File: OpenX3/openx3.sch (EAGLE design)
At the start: 34 parts, among them IC1 24AA256SN, J1 BM20B-SRDS-G-TF(LF)(SN), J2 SM12B-SRSS-TB(LF)(SN), J3 53398-0271, J4 1734260-3, U1 LC4256V-75TN100CTQFP100-L, U2 AM29F016D-70EF, U3 AM29F002BB90EI

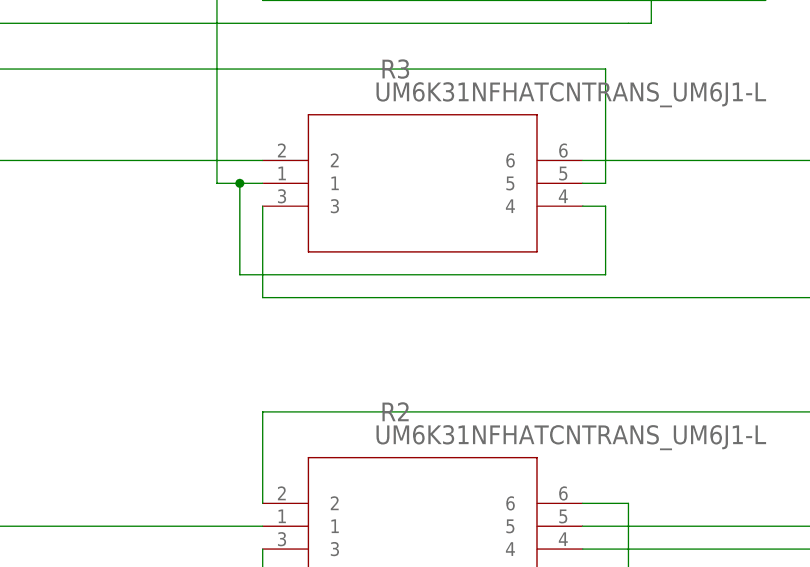
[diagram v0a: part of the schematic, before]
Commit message: Make correction where resistor arrays were not connected to +3v3, previous net name was N$4 before connecting to +3v3
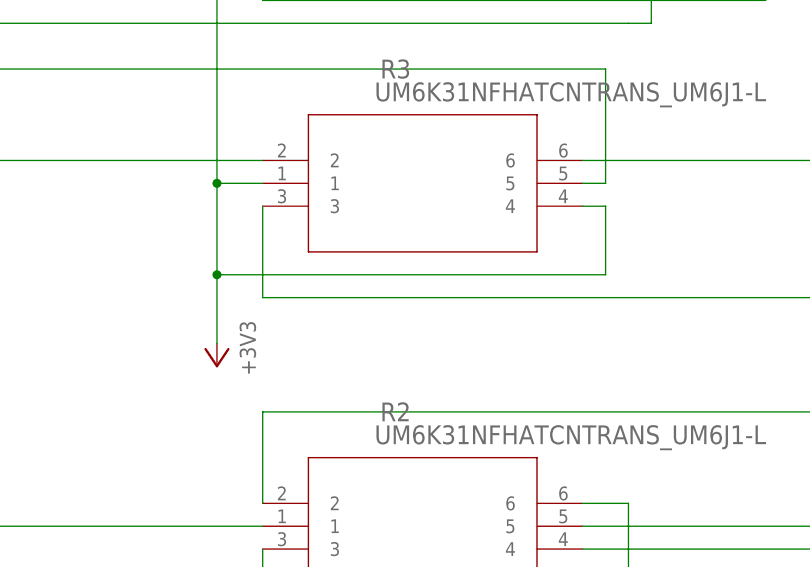
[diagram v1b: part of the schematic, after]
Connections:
- removed net N$4: R3.1, R3.4, R4.1, R4.4, R7.2, RN2A.1, RN2B.1, RN2C.1, RN2D.1
- net +3V3: now also R3.1, R3.4, R4.1, R4.4, R7.2, RN2A.1, RN2B.1, RN2C.1, RN2D.1
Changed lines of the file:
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@@
 <?xml version="1.0" encoding="utf-8"?>
 <!DOCTYPE eagle SYSTEM "eagle.dtd">
-<eagle version="9.3.1">
+<eagle version="9.5.0">
 <drawing>
 <settings>
@@
 <part name="SUPPLY12" library="supply2" library_urn="urn:adsk.eagle:library:372" deviceset="GND" device=""/>
 <part name="J1" library="BM20B-SRDS-G-TFLFSN" deviceset="BM20B-SRDS-G-TF(LF)(SN)" device=""/>
+<part name="+3V2" library="supply1" library_urn="urn:adsk.eagle:library:371" deviceset="+3V3" device=""/>
 </parts>
 <sheets>
@@
 <attribute name="NAME" x="-52.07" y="48.26" size="1.778" layer="95" align="center-left"/>
 <attribute name="VALUE" x="-52.07" y="45.72" size="1.778" layer="96" align="center-left"/>
+</instance>
+<instance part="+3V2" gate="G$1" x="-86.36" y="124.46" smashed="yes" rot="R180">
+<attribute name="VALUE" x="-83.82" y="129.54" size="1.778" layer="96" rot="R270"/>
 </instance>
 </instances>
@@
 <junction x="-99.06" y="213.36"/>
 <label x="-83.82" y="246.38" size="1.778" layer="95" rot="R90"/>
-</segment>
-</net>
-<net name="N$4" class="0">
-<segment>
-<pinref part="R4" gate="A" pin="4"/>
-<wire x1="-43.18" y1="175.26" x2="-45.72" y2="175.26" width="0.1524" layer="91"/>
-<wire x1="-43.18" y1="167.64" x2="-43.18" y2="175.26" width="0.1524" layer="91"/>
-<wire x1="-83.82" y1="167.64" x2="-43.18" y2="167.64" width="0.1524" layer="91"/>
-<pinref part="R4" gate="A" pin="1"/>
-<wire x1="-81.28" y1="177.8" x2="-83.82" y2="177.8" width="0.1524" layer="91"/>
-<wire x1="-83.82" y1="177.8" x2="-83.82" y2="167.64" width="0.1524" layer="91"/>
-<junction x="-83.82" y="177.8"/>
-<pinref part="R3" gate="A" pin="4"/>
-<wire x1="-43.18" y1="142.24" x2="-45.72" y2="142.24" width="0.1524" layer="91"/>
-<wire x1="-43.18" y1="134.62" x2="-43.18" y2="142.24" width="0.1524" layer="91"/>
-<wire x1="-83.82" y1="134.62" x2="-43.18" y2="134.62" width="0.1524" layer="91"/>
-<pinref part="R3" gate="A" pin="1"/>
-<wire x1="-81.28" y1="144.78" x2="-83.82" y2="144.78" width="0.1524" layer="91"/>
-<wire x1="-83.82" y1="144.78" x2="-83.82" y2="134.62" width="0.1524" layer="91"/>
-<junction x="-83.82" y="144.78"/>
-<wire x1="-83.82" y1="144.78" x2="-86.36" y2="144.78" width="0.1524" layer="91"/>
-<wire x1="-86.36" y1="144.78" x2="-86.36" y2="177.8" width="0.1524" layer="91"/>
-<wire x1="-86.36" y1="177.8" x2="-83.82" y2="177.8" width="0.1524" layer="91"/>
-<junction x="-86.36" y="177.8"/>
-<wire x1="-86.36" y1="198.12" x2="-86.36" y2="177.8" width="0.1524" layer="91"/>
-<pinref part="RN2" gate="D" pin="1"/>
-<wire x1="-121.92" y1="198.12" x2="-86.36" y2="198.12" width="0.1524" layer="91"/>
-<junction x="-121.92" y="198.12"/>
-<pinref part="RN2" gate="C" pin="1"/>
-<wire x1="-127" y1="198.12" x2="-121.92" y2="198.12" width="0.1524" layer="91"/>
-<junction x="-127" y="198.12"/>
-<pinref part="RN2" gate="B" pin="1"/>
-<wire x1="-132.08" y1="198.12" x2="-127" y2="198.12" width="0.1524" layer="91"/>
-<junction x="-132.08" y="198.12"/>
-<pinref part="RN2" gate="A" pin="1"/>
-<wire x1="-137.16" y1="198.12" x2="-132.08" y2="198.12" width="0.1524" layer="91"/>
-<junction x="-137.16" y="198.12"/>
-<pinref part="R7" gate="G$1" pin="2"/>
-<wire x1="-149.86" y1="198.12" x2="-137.16" y2="198.12" width="0.1524" layer="91"/>
 </segment>
 </net>
@@
 <label x="297.18" y="-132.08" size="1.778" layer="95"/>
 </segment>
-</net>
+<segment>
+<pinref part="R4" gate="A" pin="4"/>
+<wire x1="-43.18" y1="175.26" x2="-45.72" y2="175.26" width="0.1524" layer="91"/>
+<wire x1="-43.18" y1="167.64" x2="-43.18" y2="175.26" width="0.1524" layer="91"/>
+<wire x1="-83.82" y1="167.64" x2="-43.18" y2="167.64" width="0.1524" layer="91"/>
+<pinref part="R4" gate="A" pin="1"/>
+<wire x1="-81.28" y1="177.8" x2="-83.82" y2="177.8" width="0.1524" layer="91"/>
+<wire x1="-83.82" y1="177.8" x2="-83.82" y2="167.64" width="0.1524" layer="91"/>
+<junction x="-83.82" y="177.8"/>
+<pinref part="R3" gate="A" pin="4"/>
+<wire x1="-43.18" y1="142.24" x2="-45.72" y2="142.24" width="0.1524" layer="91"/>
+<wire x1="-43.18" y1="134.62" x2="-43.18" y2="142.24" width="0.1524" layer="91"/>
+<wire x1="-86.36" y1="134.62" x2="-43.18" y2="134.62" width="0.1524" layer="91"/>
+<pinref part="R3" gate="A" pin="1"/>
+<wire x1="-81.28" y1="144.78" x2="-86.36" y2="144.78" width="0.1524" layer="91"/>
+<wire x1="-86.36" y1="144.78" x2="-86.36" y2="134.62" width="0.1524" layer="91"/>
+<junction x="-86.36" y="144.78"/>
+<wire x1="-86.36" y1="144.78" x2="-86.36" y2="177.8" width="0.1524" layer="91"/>
+<wire x1="-86.36" y1="177.8" x2="-83.82" y2="177.8" width="0.1524" layer="91"/>
+<junction x="-86.36" y="177.8"/>
+<wire x1="-86.36" y1="198.12" x2="-86.36" y2="177.8" width="0.1524" layer="91"/>
+<pinref part="RN2" gate="D" pin="1"/>
+<wire x1="-121.92" y1="198.12" x2="-86.36" y2="198.12" width="0.1524" layer="91"/>
+<junction x="-121.92" y="198.12"/>
+<pinref part="RN2" gate="C" pin="1"/>
+<wire x1="-127" y1="198.12" x2="-121.92" y2="198.12" width="0.1524" layer="91"/>
+<junction x="-127" y="198.12"/>
+<pinref part="RN2" gate="B" pin="1"/>
+<wire x1="-132.08" y1="198.12" x2="-127" y2="198.12" width="0.1524" layer="91"/>
+<junction x="-132.08" y="198.12"/>
+<pinref part="RN2" gate="A" pin="1"/>
+<wire x1="-137.16" y1="198.12" x2="-132.08" y2="198.12" width="0.1524" layer="91"/>
+<junction x="-137.16" y="198.12"/>
+<pinref part="R7" gate="G$1" pin="2"/>
+<wire x1="-149.86" y1="198.12" x2="-137.16" y2="198.12" width="0.1524" layer="91"/>
+<pinref part="+3V2" gate="G$1" pin="+3V3"/>
+<wire x1="-86.36" y1="134.62" x2="-86.36" y2="127" width="0.1524" layer="91"/>
+<junction x="-86.36" y="134.62"/>
+</segment>
+</net>

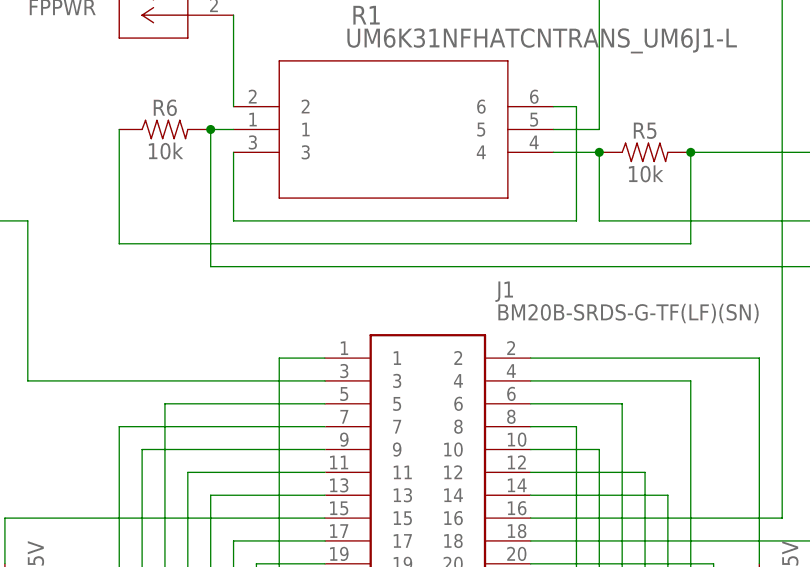
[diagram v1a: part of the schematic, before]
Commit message: fixed missing ground connection to pins 3 and 6 of transistor array for front panel power and eject inputs
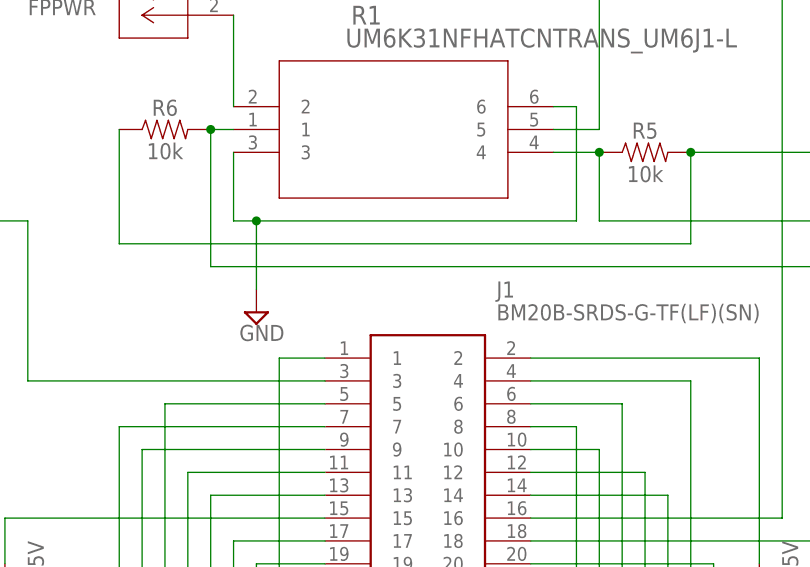
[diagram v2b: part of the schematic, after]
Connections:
- removed net N$56: R1.3, R1.6
- net GND: now also R1.3, R1.6
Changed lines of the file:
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@@
 <part name="J1" library="BM20B-SRDS-G-TFLFSN" deviceset="BM20B-SRDS-G-TF(LF)(SN)" device=""/>
 <part name="+3V2" library="supply1" library_urn="urn:adsk.eagle:library:371" deviceset="+3V3" device=""/>
+<part name="SUPPLY13" library="supply2" library_urn="urn:adsk.eagle:library:372" deviceset="GND" device=""/>
 </parts>
 <sheets>
@@
 <instance part="+3V2" gate="G$1" x="-86.36" y="124.46" smashed="yes" rot="R180">
 <attribute name="VALUE" x="-83.82" y="129.54" size="1.778" layer="96" rot="R270"/>
+</instance>
+<instance part="SUPPLY13" gate="GND" x="-78.74" y="45.72" smashed="yes">
+<attribute name="VALUE" x="-80.645" y="42.545" size="1.778" layer="96"/>
 </instance>
 </instances>
@@
 <wire x1="167.64" y1="177.8" x2="162.56" y2="177.8" width="0.1524" layer="91"/>
 <pinref part="U3" gate="A" pin="!CE"/>
-</segment>
-</net>
-<net name="N$56" class="0">
-<segment>
-<pinref part="R1" gate="A" pin="3"/>
-<wire x1="-81.28" y1="63.5" x2="-81.28" y2="55.88" width="0.1524" layer="91"/>
-<wire x1="-81.28" y1="55.88" x2="-43.18" y2="55.88" width="0.1524" layer="91"/>
-<wire x1="-43.18" y1="55.88" x2="-43.18" y2="68.58" width="0.1524" layer="91"/>
-<pinref part="R1" gate="A" pin="6"/>
-<wire x1="-43.18" y1="68.58" x2="-45.72" y2="68.58" width="0.1524" layer="91"/>
 </segment>
 </net>
@@
 <pinref part="J1" gate="G$1" pin="1"/>
 </segment>
-</net>
+<segment>
+<pinref part="R1" gate="A" pin="3"/>
+<wire x1="-81.28" y1="63.5" x2="-81.28" y2="55.88" width="0.1524" layer="91"/>
+<wire x1="-81.28" y1="55.88" x2="-78.74" y2="55.88" width="0.1524" layer="91"/>
+<wire x1="-78.74" y1="55.88" x2="-43.18" y2="55.88" width="0.1524" layer="91"/>
+<wire x1="-43.18" y1="55.88" x2="-43.18" y2="68.58" width="0.1524" layer="91"/>
+<pinref part="R1" gate="A" pin="6"/>
+<wire x1="-43.18" y1="68.58" x2="-45.72" y2="68.58" width="0.1524" layer="91"/>
+<pinref part="SUPPLY13" gate="GND" pin="GND"/>
+<wire x1="-78.74" y1="48.26" x2="-78.74" y2="55.88" width="0.1524" layer="91"/>
+<junction x="-78.74" y="55.88"/>
+</segment>
+</net>

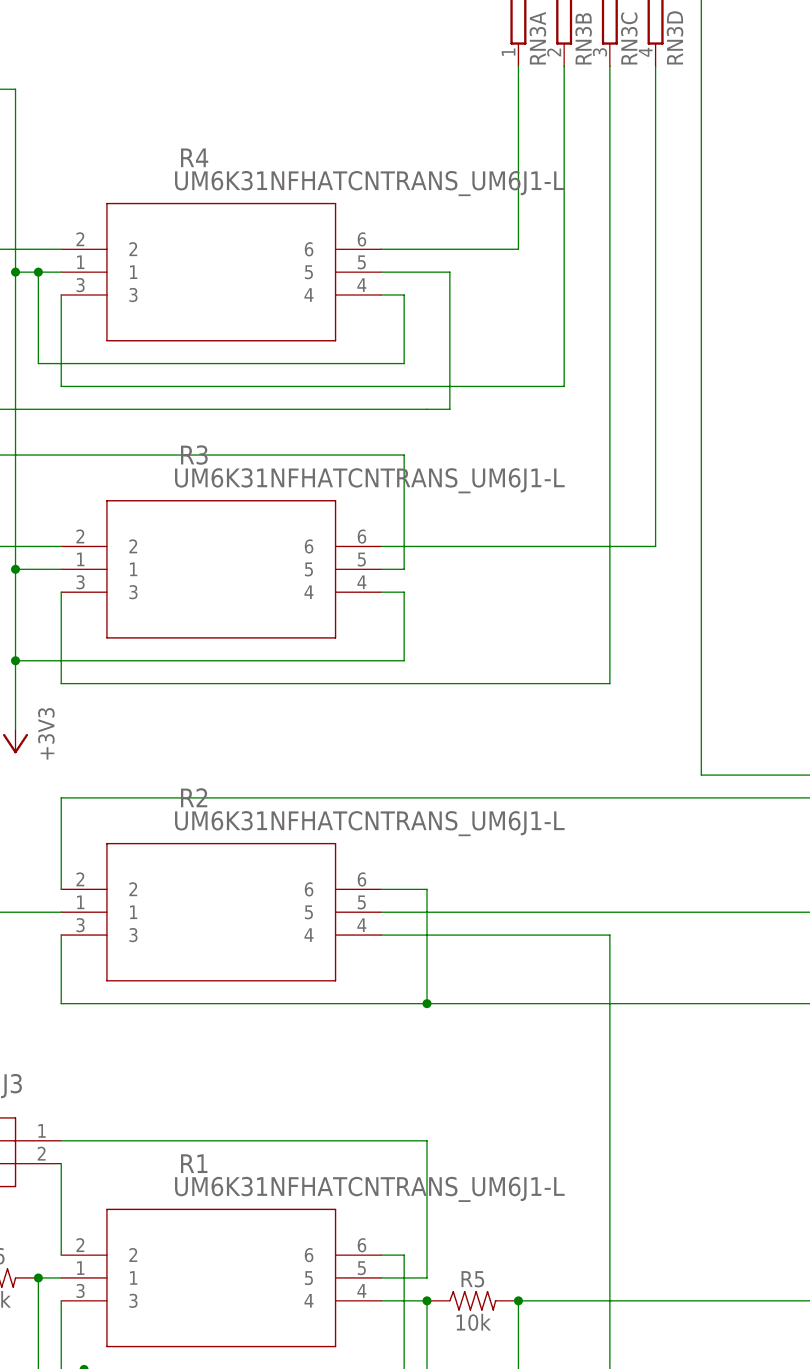
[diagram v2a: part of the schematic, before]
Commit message: Updated part # for mosfet array from Nch to Pch, possible replacement is SI1967DH-T1-GE3 but still waiting to verify. Also fixed error in DRC that cause solder mask to be missing around some components.
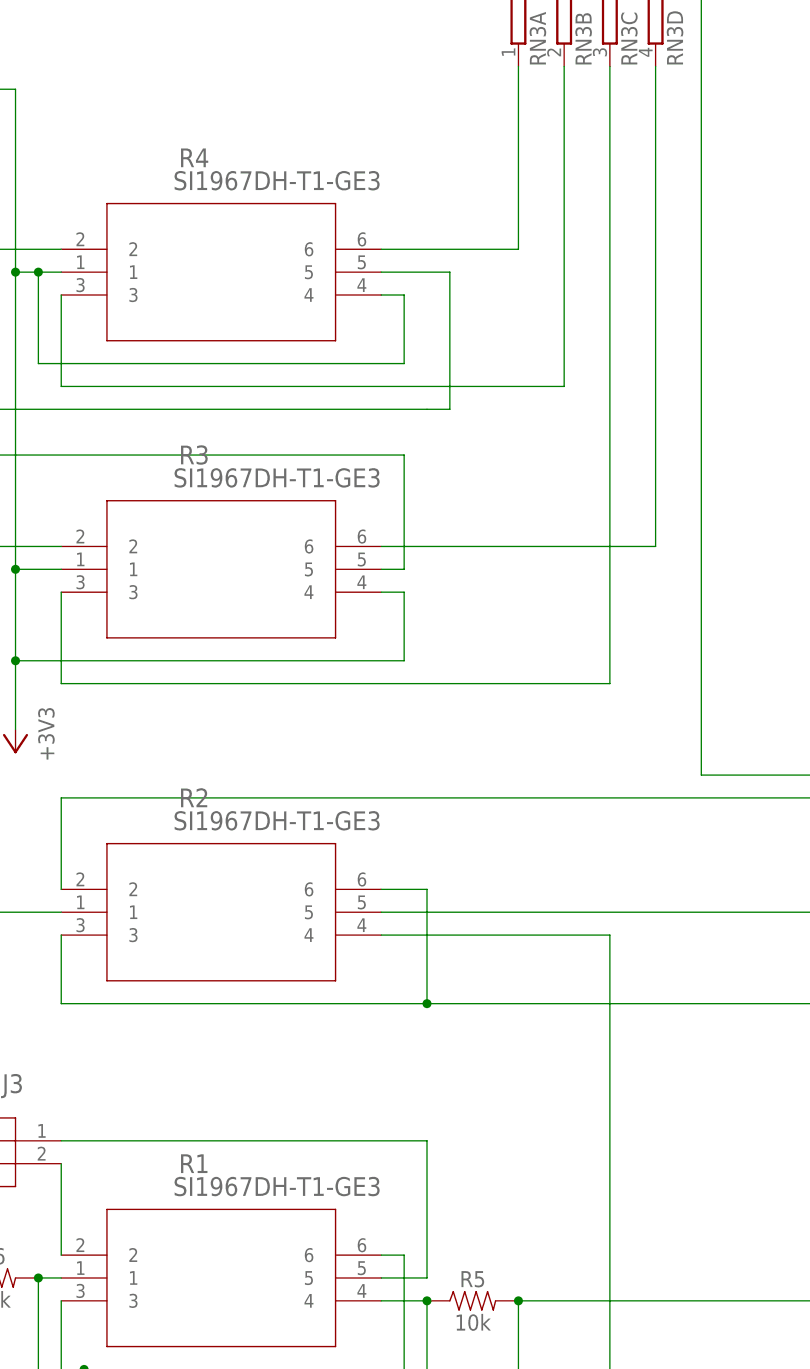
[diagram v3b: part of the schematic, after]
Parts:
- R1, R2, R3, R4: value UM6K31NFHATCNTRANS_UM6J1-L -> SI1967DH-T1-GE3
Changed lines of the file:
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@@
 <?xml version="1.0" encoding="utf-8"?>
 <!DOCTYPE eagle SYSTEM "eagle.dtd">
-<eagle version="9.5.0">
+<eagle version="9.5.2">
 <drawing>
 <settings>
@@
 <part name="U2" library="AM29F016D-70EF" deviceset="AM29F016D-70EF" device=""/>
 <part name="JP1" library="pinhead" library_urn="urn:adsk.eagle:library:325" deviceset="PINHD-2X8" device="" package3d_urn="urn:adsk.eagle:package:22481/2"/>
-<part name="R1" library="UM6K31NFHA" deviceset="UM6K31NFHATCN" device="TRANS_UM6J1-L"/>
-<part name="R2" library="UM6K31NFHA" deviceset="UM6K31NFHATCN" device="TRANS_UM6J1-L"/>
-<part name="R3" library="UM6K31NFHA" deviceset="UM6K31NFHATCN" device="TRANS_UM6J1-L"/>
-<part name="R4" library="UM6K31NFHA" deviceset="UM6K31NFHATCN" device="TRANS_UM6J1-L"/>
+<part name="R1" library="UM6K31NFHA" deviceset="UM6K31NFHATCN" device="TRANS_UM6J1-L" value="SI1967DH-T1-GE3"/>
+<part name="R2" library="UM6K31NFHA" deviceset="UM6K31NFHATCN" device="TRANS_UM6J1-L" value="SI1967DH-T1-GE3"/>
+<part name="R3" library="UM6K31NFHA" deviceset="UM6K31NFHATCN" device="TRANS_UM6J1-L" value="SI1967DH-T1-GE3"/>
+<part name="R4" library="UM6K31NFHA" deviceset="UM6K31NFHATCN" device="TRANS_UM6J1-L" value="SI1967DH-T1-GE3"/>
 <part name="R5" library="SparkFun-Resistors" library_urn="urn:adsk.eagle:library:532" deviceset="10KOHM" device="-0603-1/10W-1%" package3d_urn="urn:adsk.eagle:package:39650/1" value="10k"/>
 <part name="R6" library="SparkFun-Resistors" library_urn="urn:adsk.eagle:library:532" deviceset="10KOHM" device="-0603-1/10W-1%" package3d_urn="urn:adsk.eagle:package:39650/1" value="10k"/>
